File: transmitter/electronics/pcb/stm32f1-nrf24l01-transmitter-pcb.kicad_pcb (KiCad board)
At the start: 2 copper layers, 29 parts, among them K1 CONN_3, K10 CONN_3, K11 CONN_3, K2 CONN_3, K3 CONN_3, K4 CONN_3, K5 CONN_3, K6 CONN_3, K7 CONN_3, K8 CONN_3, K9 CONN_3, P1 Charge, P2 LED, P3 CONN_2, P4 CONN_2, P5 CONN_4, Q1 BC548, SW1 ON/OFF, U1 LIPO_CHARGER_+_PROTECTION, U2 STM32F103C8T6_DEV_BOARD, U3 NRF24L01P

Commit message: Work on PCB
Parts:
- removed BT1: BATTERY, PIN_ARRAY_2X1
- removed K1, K10, K11, K2, K3, K4, K5, K6, K7, K8, K9: CONN_3, PIN_ARRAY_3X1
- removed P1: Charge, PIN_ARRAY_2X1
- removed P2: LED, PIN_ARRAY_2X1
- removed P3, P4: CONN_2, PIN_ARRAY_2X1
- removed P5: CONN_4, PIN_ARRAY_4x1
- removed SW1: ON/OFF, PIN_ARRAY_2X1
- added C3: 1u, Capacitor_SMD:C_0805_2012Metric_Pad1.15x1.40mm_HandSolder, F.Cu at (154.9, 95.2)
- added C4: 1u, Capacitor_SMD:C_0805_2012Metric_Pad1.15x1.40mm_HandSolder, F.Cu at (95.2, 57.1)
- added H1: MountingHole, MountingHole:MountingHole_3.2mm_M3_DIN965, F.Cu at (182.9, 54.6)
- added H2: MountingHole, MountingHole:MountingHole_3.2mm_M3_DIN965, F.Cu at (182.9, 95.2)
- added J1: PA1/A1, Connector_JST:JST_EH_B3B-EH-A_1x03_P2.50mm_Vertical, F.Cu at (152.4, 55.9)
- added J10: PB3, Connector_JST:JST_EH_B3B-EH-A_1x03_P2.50mm_Vertical, F.Cu at (124.5, 96.5)
- added J11: PB4, Connector_JST:JST_EH_B3B-EH-A_1x03_P2.50mm_Vertical, F.Cu at (129.5, 96.5)
- added J12: PB5, Connector_JST:JST_EH_B3B-EH-A_1x03_P2.50mm_Vertical, F.Cu at (134.6, 96.5)
- added J13: PB6, Connector_JST:JST_EH_B3B-EH-A_1x03_P2.50mm_Vertical, F.Cu at (139.7, 96.5)
- added J14: PB7, Connector_JST:JST_EH_B3B-EH-A_1x03_P2.50mm_Vertical, F.Cu at (144.8, 96.5)
- added J15: PB8, Connector_JST:JST_EH_B3B-EH-A_1x03_P2.50mm_Vertical, F.Cu at (149.9, 96.5)
- added J16: PB10, Connector_JST:JST_EH_B3B-EH-A_1x03_P2.50mm_Vertical, F.Cu at (106.7, 55.9)
- added J17: PB11, Connector_JST:JST_EH_B3B-EH-A_1x03_P2.50mm_Vertical, F.Cu at (101.6, 55.9)
- added J18: USB, Connector_JST:JST_EH_B4B-EH-A_1x04_P2.50mm_Vertical, F.Cu at (118.1, 94.0)
- added J19: BATTERY, Connector_JST:JST_EH_B2B-EH-A_1x02_P2.50mm_Vertical, F.Cu at (184.2, 73.7)
- added J2: PA2/A2, Connector_JST:JST_EH_B3B-EH-A_1x03_P2.50mm_Vertical, F.Cu at (147.3, 55.9)
- added J20: UART, Connector_PinHeader_2.54mm:PinHeader_1x03_P2.54mm_Vertical, F.Cu at (96.5, 92.7)
- added J21: SWITCH, Connector_JST:JST_EH_B2B-EH-A_1x02_P2.50mm_Vertical, F.Cu at (184.2, 83.8)
- added J22: NRF24 connector, Connector_JST:JST_EH_B7B-EH-A_1x07_P2.50mm_Vertical, F.Cu at (96.5, 68.6)
- added J23: Buzzer, Connector_JST:JST_EH_B2B-EH-A_1x02_P2.50mm_Vertical, F.Cu at (170.2, 96.5)
- added J24: Meter, Connector_JST:JST_EH_B2B-EH-A_1x02_P2.50mm_Vertical, F.Cu at (158.8, 96.5)
- added J25: LED, Connector_JST:JST_EH_B2B-EH-A_1x02_P2.50mm_Vertical, F.Cu at (157.5, 61.0)
- added J26: Red, TestPoint:TestPoint_Pad_1.5x1.5mm, F.Cu at (179.1, 63.5)
- added J27: Blue, TestPoint:TestPoint_Pad_1.5x1.5mm, F.Cu at (179.1, 61.0)
- added J28: Charger LED, Connector_JST:JST_EH_B3B-EH-A_1x03_P2.50mm_Vertical, F.Cu at (184.2, 61.0)
- added J3: PA3/A3, Connector_JST:JST_EH_B3B-EH-A_1x03_P2.50mm_Vertical, F.Cu at (142.2, 55.9)
- added J4: PA4/A4, Connector_JST:JST_EH_B3B-EH-A_1x03_P2.50mm_Vertical, F.Cu at (137.2, 55.9)
- added J5: PA5/A5, Connector_JST:JST_EH_B3B-EH-A_1x03_P2.50mm_Vertical, F.Cu at (132.1, 55.9)
- added J6: PA6/A6, Connector_JST:JST_EH_B3B-EH-A_1x03_P2.50mm_Vertical, F.Cu at (127.0, 55.9)
- added J7: PA7/A7, Connector_JST:JST_EH_B3B-EH-A_1x03_P2.50mm_Vertical, F.Cu at (121.9, 55.9)
- added J8: PB0/A8, Connector_JST:JST_EH_B3B-EH-A_1x03_P2.50mm_Vertical, F.Cu at (116.8, 55.9)
- added J9: PB1/A9, Connector_JST:JST_EH_B3B-EH-A_1x03_P2.50mm_Vertical, F.Cu at (111.8, 55.9)
- added R5: 1k, Resistor_SMD:R_0805_2012Metric_Pad1.15x1.40mm_HandSolder, F.Cu at (149.9, 66.0)
- C1: value 1u -> 100nF; footprint SM0805 -> Capacitor_SMD:C_0805_2012Metric_Pad1.15x1.40mm_HandSolder; moved to F.Cu
- C2: value 100nF -> 1u; footprint SM0805 -> Capacitor_SMD:C_0805_2012Metric_Pad1.15x1.40mm_HandSolder; moved to F.Cu
- Q1: value BC548 -> BC547B; footprint TO92 -> Package_TO_SOT_SMD:SOT-23_Handsoldering
- R1: value 1k -> 22k; footprint SM0805 -> Resistor_SMD:R_0805_2012Metric_Pad1.15x1.40mm_HandSolder; moved to F.Cu
- R2: value R -> 33k; footprint SM0805 -> Resistor_SMD:R_0805_2012Metric_Pad1.15x1.40mm_HandSolder; moved to F.Cu
- R3: value R -> 1k; footprint SM0805 -> Resistor_SMD:R_0805_2012Metric_Pad1.15x1.40mm_HandSolder; moved to F.Cu
- R4: value 1k -> 3k9; footprint SM0805 -> Resistor_SMD:R_0805_2012Metric_Pad1.15x1.40mm_HandSolder; moved to F.Cu
- SP1: footprint PIN_ARRAY_2X1 -> Buzzer_Beeper:Buzzer_12x9.5RM7.6
- U1: footprint LiPo_charger_and_protection -> WLA:LiPo_charger_and_protection
- U2: footprint DIP-40__600 -> WLA:STM32F103C8T6_DEV_BOARD
- U3: footprint NRF24L01P-PA-LNA -> Connector_PinHeader_2.54mm:PinHeader_2x04_P2.54mm_Vertical; moved to F.Cu
- moved U1 168.1 mm to (170.2, 66.0), turned to 270 degrees
- moved U3 135.9 mm to (94.0, 71.1), turned to 0 degrees
- moved R1 134.7 mm to (142.2, 76.2), turned to 90 degrees
- moved R2 132.8 mm to (147.3, 76.2), turned to 270 degrees
- moved U2 132.3 mm to (127.0, 76.2)
- moved C2 121.7 mm to (160.0, 83.8), turned to 90 degrees
- moved R3 111.2 mm to (170.2, 83.8), turned to 0 degrees
- moved SP1 107.9 mm to (165.1, 91.4), turned to 0 degrees
- moved R4 103.4 mm to (156.2, 88.9)
- moved Q1 101.1 mm to (165.1, 83.8), turned to 180 degrees
- moved C1 89.1 mm to (149.9, 76.2), turned to 270 degrees
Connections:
- C1 pad 1: VCC -> /ADC0
- C2 pad 1: /ADC0 -> VDD
- Q1 pad 1: GND -> Net-(J23-Pad1)
- Q1 pad 2: N-0000013 -> Net-(Q1-Pad2)
- Q1 pad 3: N-0000014 -> GND
- R1 pad 1: N-0000043 -> VDD
- R1 pad 2: /LED -> /ADC0
- R2 pad 1: VDD -> /ADC0
- R2 pad 2: /ADC0 -> GND
- R3 pad 1: /ADC0 -> Net-(Q1-Pad2)
- R3 pad 2: GND -> /BUZZER
- R4 pad 1: /BUZZER -> /METER
- R4 pad 2: N-0000013 -> Net-(C3-Pad1)
- SP1 pad 2: N-0000014 -> Net-(J23-Pad1)
- U1 pad 4: N-0000029 -> GND
- U1 pad 5: N-000004 -> /+USB
- U1 pad 6: N-0000021 -> GND
- U2 pad 11: (no net) -> /PB3
- U2 pad 12: (no net) -> /PB4
- U2 pad 13: (no net) -> /PB5
- U2 pad 14: (no net) -> /PB6
- U2 pad 15: (no net) -> /PB7
- U2 pad 16: (no net) -> /PB8
- U2 pad 17: (no net) -> /METER
- U2 pad 20: N-0000022 -> VCC
- U2 pad 21: N-0000022 -> VCC
- U2 pad 23: (no net) -> Net-(U2-Pad23)
- U2 pad 24: (no net) -> Net-(U2-Pad24)
- U2 pad 26: /ADC1 -> /PA1/ADC1
- U2 pad 27: /ADC2 -> /PA2/ADC2
- U2 pad 28: /ADC3 -> /PA3/ADC3
- U2 pad 29: /ADC4 -> /PA4/ADC4
- U2 pad 30: /ADC5 -> /PA5/ADC5
- U2 pad 31: /ADC6 -> /PA6/ADC6
- U2 pad 32: /ADC7 -> /PA7/ADC7
- U2 pad 33: /ADC8 -> /PB0/ADC8
- U2 pad 34: /ADC9 -> /PB1/ADC9
- U2 pad 35: /SW2 -> /PB10
- U2 pad 36: /SW1 -> /PB11
- U2 pad 37: (no net) -> Net-(U2-Pad37)
- U2 pad 8: (no net) -> /USBDM
- U2 pad 9: (no net) -> /USBDP
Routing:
- net GND: track 122.4 -> 12.5 mm, vias 4 -> 0
- net VCC: track 122.5 -> 16.1 mm, vias 2 -> 0
- net /ADC0: track 20.5 -> 0.00 mm
- net N-0000022: track 15.2 -> 0.00 mm
- net N-0000014: track 15.2 -> 0.00 mm
- net VDD: track 12.4 -> 0.00 mm
- net /MISO: track 27.9 -> 16.1 mm, vias 2 -> 0
- net N-0000029: track 8.45 -> 0.00 mm
- net /SCK: track 33.0 -> 24.7 mm, vias 2 -> 0
- net N-000004: track 7.82 -> 0.00 mm
- net N-0000021: track 7.82 -> 0.00 mm
- net N-0000028: track 6.61 -> 0.00 mm
- net /SW2: track 5.08 -> 0.00 mm
- net /SW1: track 5.08 -> 0.00 mm
- net /ADC9: track 5.08 -> 0.00 mm
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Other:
- board outline added: 97.8 x 49.5 mm
- net class Default: clearance 0.1016 -> 0.2; trace_width 0.254 -> 0.25; via_dia 0.889 -> 0.8; via_drill 0.635 -> 0.4
- rule trace_clearance: 0.1016 -> 0.2
- rule trace_min: 0.254 -> 0.2
- rule via_min_drill: 0.508 -> 0.3
- rule via_min_size: 0.889 -> 0.4
- board text removed: "IMPORTANT: the nRF module is on the back side, i.e mirrored!"

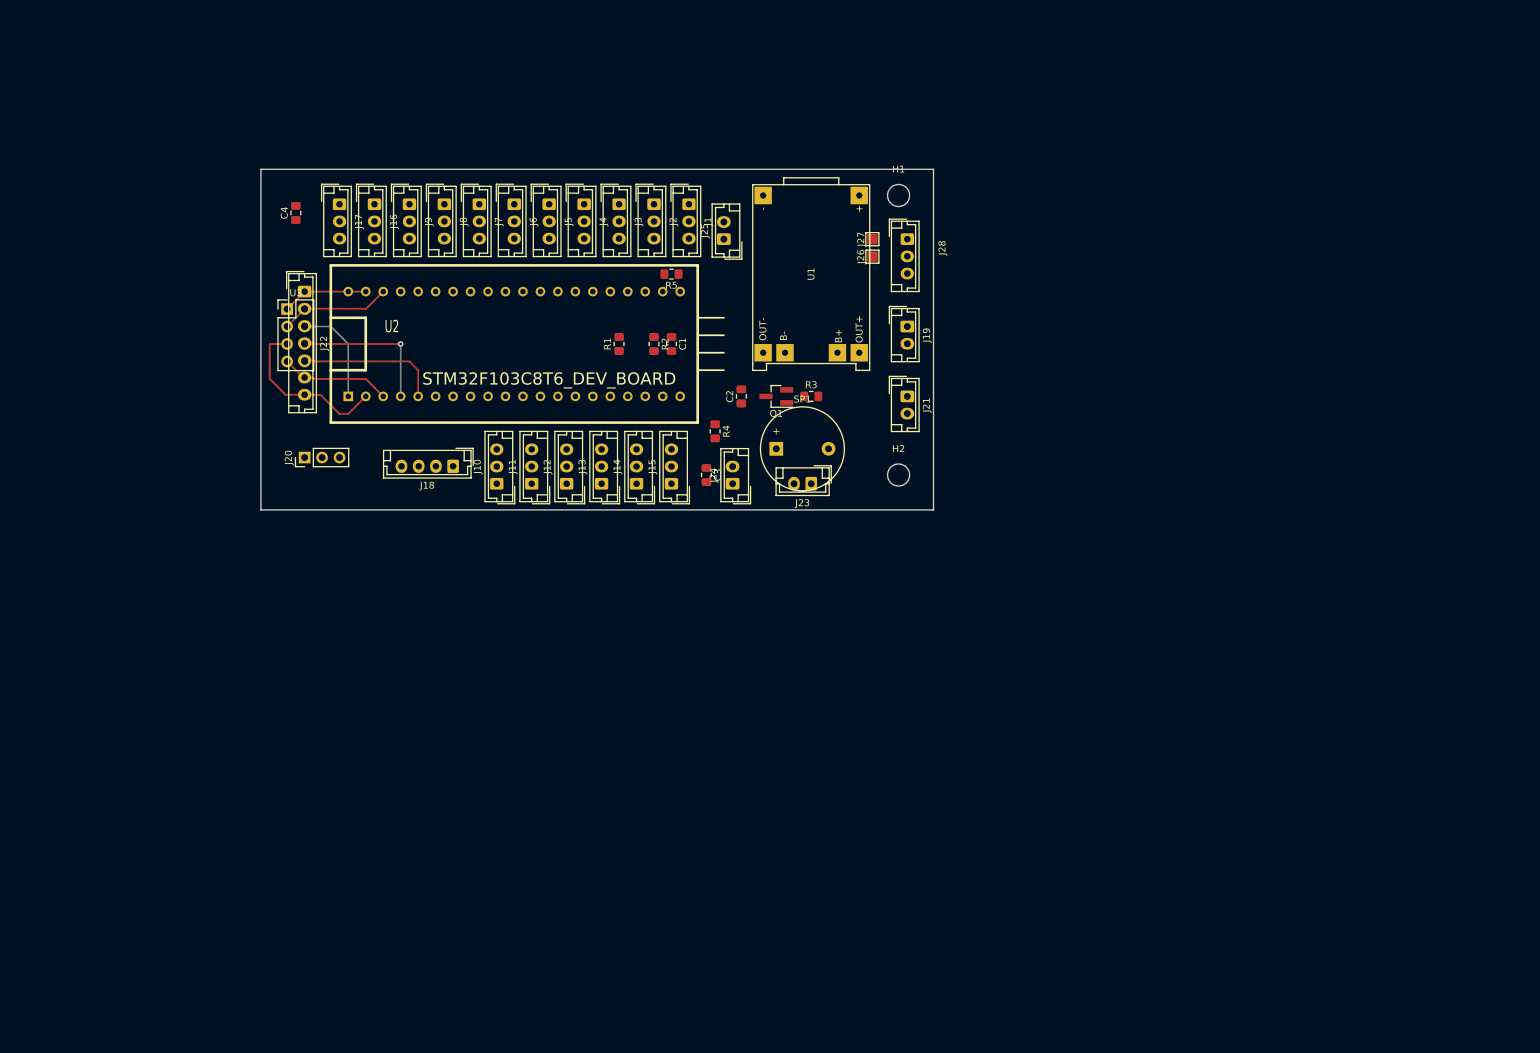
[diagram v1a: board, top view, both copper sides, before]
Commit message: Update PCB without Blue Pill, but use STM32F103 directly
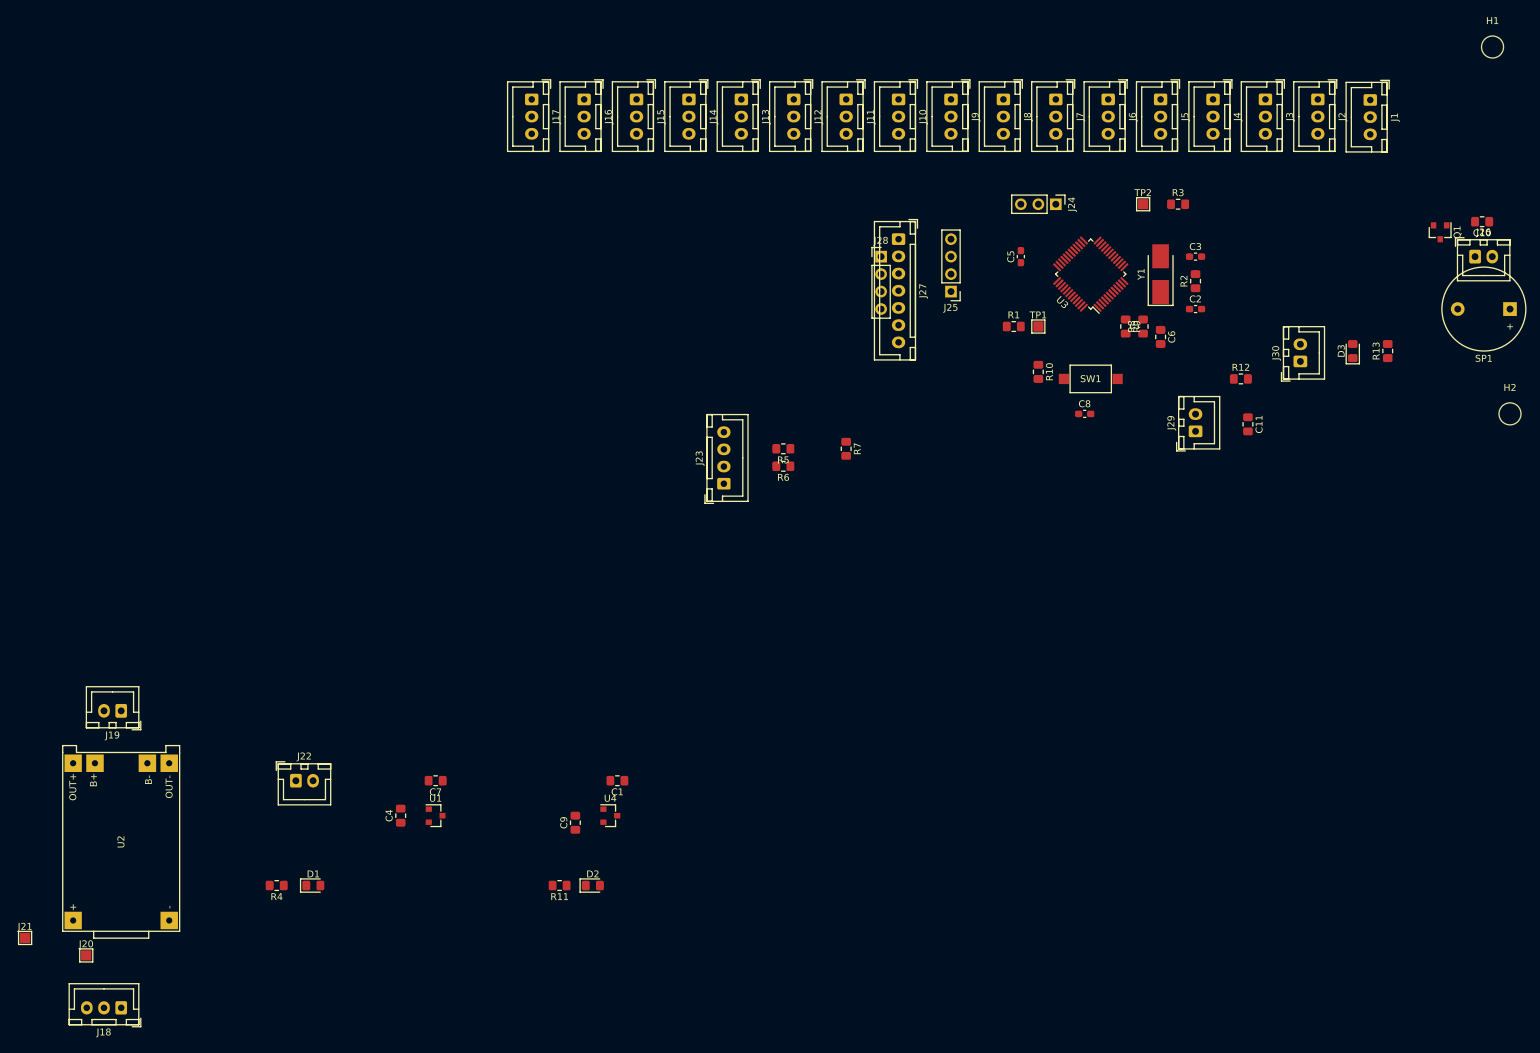
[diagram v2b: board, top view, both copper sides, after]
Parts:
- added C10: 1u, Capacitor_SMD:C_0805_2012Metric_Pad1.15x1.40mm_HandSolder, F.Cu at (267.7, 58.4)
- added C11: 1u, Capacitor_SMD:C_0805_2012Metric_Pad1.15x1.40mm_HandSolder, F.Cu at (233.7, 87.9)
- added C5: 100n, Capacitor_SMD:C_0603_1608Metric_Pad1.05x0.95mm_HandSolder, F.Cu at (200.7, 63.5)
- added C6: 100nF, Capacitor_SMD:C_0805_2012Metric_Pad1.15x1.40mm_HandSolder, F.Cu at (221.0, 75.2)
- added C7: 1u, Capacitor_SMD:C_0805_2012Metric_Pad1.15x1.40mm_HandSolder, F.Cu at (115.6, 139.7)
- added C8: 100n, Capacitor_SMD:C_0603_1608Metric_Pad1.05x0.95mm_HandSolder, F.Cu at (209.9, 86.4)
- added C9: 47u, Capacitor_SMD:C_0805_2012Metric_Pad1.15x1.40mm_HandSolder, F.Cu at (135.9, 145.8)
- added D1: LED, LED_SMD:LED_0805_2012Metric_Pad1.15x1.40mm_HandSolder, F.Cu at (97.8, 154.9)
- added D2: LED, LED_SMD:LED_0805_2012Metric_Pad1.15x1.40mm_HandSolder, F.Cu at (138.4, 154.9)
- added D3: LED, LED_SMD:LED_0805_2012Metric_Pad1.15x1.40mm_HandSolder, F.Cu at (248.9, 77.2)
- added J29: Meter, Connector_JST:JST_XH_B2B-XH-A_1x02_P2.50mm_Vertical, F.Cu at (226.1, 88.9)
- added J30: LED, Connector_JST:JST_XH_B2B-XH-A_1x02_P2.50mm_Vertical, F.Cu at (241.3, 78.7)
- added R10: 10k, Resistor_SMD:R_0805_2012Metric_Pad1.15x1.40mm_HandSolder, F.Cu at (203.2, 80.3)
- added R11: 1k5, Resistor_SMD:R_0805_2012Metric_Pad1.15x1.40mm_HandSolder, F.Cu at (133.6, 154.9)
- added R12: 3k9, Resistor_SMD:R_0805_2012Metric_Pad1.15x1.40mm_HandSolder, F.Cu at (232.7, 81.3)
- added R13: 1k, Resistor_SMD:R_0805_2012Metric_Pad1.15x1.40mm_HandSolder, F.Cu at (254.0, 77.2)
- added R6: 18, Resistor_SMD:R_0805_2012Metric_Pad1.15x1.40mm_HandSolder, F.Cu at (166.1, 94.0)
- added R7: 1K5, Resistor_SMD:R_0805_2012Metric_Pad1.15x1.40mm_HandSolder, F.Cu at (175.3, 91.4)
- added R8: 22k, Resistor_SMD:R_0805_2012Metric_Pad1.15x1.40mm_HandSolder, F.Cu at (218.4, 73.7)
- added R9: 33k, Resistor_SMD:R_0805_2012Metric_Pad1.15x1.40mm_HandSolder, F.Cu at (215.9, 73.7)
- added SW1: RESET, tact-switch:Tact switch 6x4x3, F.Cu at (210.8, 81.3)
- added TP1: BOOT0, TestPoint:TestPoint_Pad_1.5x1.5mm, F.Cu at (203.2, 73.7)
- added TP2: BOOT1, TestPoint:TestPoint_Pad_1.5x1.5mm, F.Cu at (218.4, 55.9)
- added U4: MCP1703A-3302, Package_TO_SOT_SMD:SOT-23, F.Cu at (141.0, 144.8)
- added Y1: 8MHz, Crystal:Crystal_SMD_5032-2Pin_5.0x3.2mm_HandSoldering, F.Cu at (221.0, 66.0)
- C1: value 100nF -> 1u
- C2, C3: value 1u -> 18p; footprint Capacitor_SMD:C_0805_2012Metric_Pad1.15x1.40mm_HandSolder -> Capacitor_SMD:C_0603_1608Metric_Pad1.05x0.95mm_HandSolder
- C4: value 1u -> 10u
- J1, J10, J11, J12, J13, J14, J15, J16, J17, J2, J3, J4, J5, J6, J7, J8, J9: footprint Connector_JST:JST_EH_B3B-EH-A_1x03_P2.50mm_Vertical -> Connector_JST:JST_XH_B3B-XH-A_1x03_P2.50mm_Vertical
- J18: value USB -> External charger LED; footprint Connector_JST:JST_EH_B4B-EH-A_1x04_P2.50mm_Vertical -> Connector_JST:JST_XH_B3B-XH-A_1x03_P2.50mm_Vertical
- J19: footprint Connector_JST:JST_EH_B2B-EH-A_1x02_P2.50mm_Vertical -> Connector_JST:JST_XH_B2B-XH-A_1x02_P2.50mm_Vertical
- J20: value UART -> Red; footprint Connector_PinHeader_2.54mm:PinHeader_1x03_P2.54mm_Vertical -> TestPoint:TestPoint_Pad_1.5x1.5mm
- J21: value SWITCH -> Blue; footprint Connector_JST:JST_EH_B2B-EH-A_1x02_P2.50mm_Vertical -> TestPoint:TestPoint_Pad_1.5x1.5mm
- J22: value NRF24 connector -> POWER SWITCH; footprint Connector_JST:JST_EH_B7B-EH-A_1x07_P2.50mm_Vertical -> Connector_JST:JST_XH_B2B-XH-A_1x02_P2.50mm_Vertical
- J23: value Buzzer -> USB; footprint Connector_JST:JST_EH_B2B-EH-A_1x02_P2.50mm_Vertical -> Connector_JST:JST_XH_B4B-XH-A_1x04_P2.50mm_Vertical
- J24: value Meter -> UART; footprint Connector_JST:JST_EH_B2B-EH-A_1x02_P2.50mm_Vertical -> Connector_PinHeader_2.54mm:PinHeader_1x03_P2.54mm_Vertical
- J25: value LED -> SWD; footprint Connector_JST:JST_EH_B2B-EH-A_1x02_P2.50mm_Vertical -> Connector_PinHeader_2.54mm:PinHeader_1x04_P2.54mm_Vertical
- J26: value Red -> Buzzer; footprint TestPoint:TestPoint_Pad_1.5x1.5mm -> Connector_JST:JST_XH_B2B-XH-A_1x02_P2.50mm_Vertical
- J27: value Blue -> NRF24 connector; footprint TestPoint:TestPoint_Pad_1.5x1.5mm -> Connector_JST:JST_XH_B7B-XH-A_1x07_P2.50mm_Vertical
- J28: value Charger LED -> NRF24 module; footprint Connector_JST:JST_EH_B3B-EH-A_1x03_P2.50mm_Vertical -> Connector_PinHeader_2.54mm:PinHeader_1x04_P2.54mm_Vertical
- Q1: value BC547B -> PMV30UN; footprint Package_TO_SOT_SMD:SOT-23_Handsoldering -> Package_TO_SOT_SMD:SOT-23
- R1: value 22k -> 100k
- R2: value 33k -> 10M
- R3: value 1k -> 100k
- R4: value 3k9 -> 1k5
- R5: value 1k -> 18
- U1: value LIPO_CHARGER_+_PROTECTION -> MCP1703A-3302; footprint WLA:LiPo_charger_and_protection -> Package_TO_SOT_SMD:SOT-23
- U2: value STM32F103C8T6_DEV_BOARD -> LIPO_CHARGER_+_PROTECTION; footprint WLA:STM32F103C8T6_DEV_BOARD -> WLA:LiPo_charger_and_protection
- U3: value NRF24L01P -> STM32F103CBT6; footprint Connector_PinHeader_2.54mm:PinHeader_2x04_P2.54mm_Vertical -> Package_QFP:LQFP-48_7x7mm_P0.5mm
- moved J21 150.5 mm to (55.9, 162.6), turned to 0 degrees
- moved J19 127.2 mm to (69.8, 129.5), turned to 180 degrees
- moved U3 117.0 mm to (210.8, 66.0), turned to 135 degrees
- moved SP1 108.6 mm to (271.8, 71.1), turned to 180 degrees
- moved J1 100.2 mm to (251.5, 40.7)
- moved Q1 99.4 mm to (261.6, 60.0), turned to 270 degrees
- moved J2 97.7 mm to (243.8, 40.6)
- moved U1 95.8 mm to (115.6, 144.8), turned to 0 degrees
- moved J3 95.2 mm to (236.2, 40.6)
- moved J4 92.7 mm to (228.6, 40.6)
- moved J18 92.4 mm to (69.8, 172.7)
- moved U2 92.2 mm to (69.8, 148.6), turned to 90 degrees
- moved R4 91.8 mm to (92.5, 154.9), turned to 180 degrees
- moved J5 90.2 mm to (221.0, 40.6)
- moved H2 89.3 mm to (271.8, 86.4)
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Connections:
- C1 pad 1: /ADC0 -> VDD
- C2 pad 1: VDD -> /OSCIN
- C3 pad 1: Net-(C3-Pad1) -> /OSCOUT
- C4 pad 1: VCC -> +3V3
- J1 pad 2: VCC -> +3V3
- J1 pad 3: /PA1/ADC1 -> /PA1-ADC1
- J10 pad 2: VCC -> +3V3
- J11 pad 2: VCC -> +3V3
- J12 pad 2: VCC -> +3V3
- J13 pad 2: VCC -> +3V3
- J14 pad 2: VCC -> +3V3
- J15 pad 2: VCC -> +3V3
- J16 pad 2: VCC -> +3V3
- J17 pad 2: VCC -> +3V3
- J18 pad 1: GND -> Net-(J18-Pad1)
- J18 pad 2: /USBDP -> Net-(J18-Pad2)
- J18 pad 3: /USBDM -> /+USB
- J2 pad 2: VCC -> +3V3
- J2 pad 3: /PA2/ADC2 -> /PA2-ADC2
- J20 pad 1: GND -> Net-(J18-Pad2)
- J21 pad 1: Net-(J21-Pad1) -> Net-(J18-Pad1)
- J22 pad 1: GND -> Net-(J22-Pad1)
- J22 pad 2: VCC -> VDD
- J23 pad 1: Net-(J23-Pad1) -> GND
- J23 pad 2: VDD -> Net-(J23-Pad2)
- J24 pad 2: Net-(C3-Pad1) -> /TX
- J25 pad 1: Net-(J25-Pad1) -> GND
- J25 pad 2: VCC -> /SWDCLK
- J27 pad 1: Net-(J27-Pad1) -> GND
- J28 pad 1: Net-(J27-Pad1) -> GND
- J28 pad 2: Net-(J26-Pad1) -> /CE
- J28 pad 3: /+USB -> /SCK
- J3 pad 2: VCC -> +3V3
- J3 pad 3: /PA3/ADC3 -> /PA3-ADC3
- J4 pad 2: VCC -> +3V3
- J4 pad 3: /PA4/ADC4 -> /PA4-ADC4
- J5 pad 2: VCC -> +3V3
- J5 pad 3: /PA5/ADC5 -> /PA5-ADC5
- J6 pad 2: VCC -> +3V3
- J6 pad 3: /PA6/ADC6 -> /PA6-ADC6
- J7 pad 2: VCC -> +3V3
- J7 pad 3: /PA7/ADC7 -> /PA7-ADC7
- J8 pad 2: VCC -> +3V3
- J8 pad 3: /PB0/ADC8 -> /PB0-ADC8
- J9 pad 2: VCC -> +3V3
- J9 pad 3: /PB1/ADC9 -> /PB1-ADC9
- Q1 pad 1: Net-(J23-Pad1) -> /BUZZER
- Q1 pad 2: Net-(Q1-Pad2) -> GND
- Q1 pad 3: GND -> Net-(J26-Pad1)
- R1 pad 1: VDD -> /BOOT0
- R1 pad 2: /ADC0 -> GND
- R2 pad 1: /ADC0 -> /OSCIN
- R2 pad 2: GND -> /OSCOUT
- R3 pad 1: Net-(Q1-Pad2) -> /BOOT1
- R3 pad 2: /BUZZER -> GND
- R4 pad 1: /METER -> Net-(D1-Pad1)
- R4 pad 2: Net-(C3-Pad1) -> GND
- R5 pad 1: Net-(J25-Pad1) -> /USBDM
- R5 pad 2: /LED -> Net-(J23-Pad3)
- SP1 pad 2: Net-(J23-Pad1) -> Net-(J26-Pad1)
- U1 pad 1: Net-(J19-Pad2) -> GND
- U1 pad 2: Net-(J19-Pad1) -> +3V3
- U1 pad 3: Net-(J21-Pad1) -> VDD
- U2 pad 1: /CSN -> Net-(J19-Pad2)
- U2 pad 2: /SCK -> Net-(J19-Pad1)
- U2 pad 3: /MISO -> Net-(J22-Pad1)
- U2 pad 4: /MOSI -> GND
- U2 pad 5: /IRQ -> /+USB
- U2 pad 6: /TX -> GND
- U3 pad 1: GND -> +3V3
- U3 pad 2: VCC -> /LED
- U3 pad 3: VCC -> Net-(U3-Pad3)
- U3 pad 4: /CSN -> Net-(U3-Pad4)
- U3 pad 5: /SCK -> /OSCIN
- U3 pad 6: /MOSI -> /OSCOUT
- U3 pad 7: /MISO -> /NRST
- U3 pad 8: /IRQ -> GND
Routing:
- net /SCK: track 24.7 -> 0.00 mm
- net /MOSI: track 23.0 -> 0.00 mm, vias 1 -> 0
- net /IRQ: track 20.9 -> 0.00 mm
- net VCC: track 16.1 -> 0.00 mm
- net /MISO: track 16.1 -> 0.00 mm
- net /CSN: track 15.0 -> 0.00 mm
- net GND: track 12.5 -> 0.00 mm
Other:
- board outline removed

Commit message: Work on schematics and layout
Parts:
- removed J28: NRF24 module, Connector_PinHeader_2.54mm:PinHeader_1x04_P2.54mm_Vertical
- J25: footprint Connector_PinHeader_2.54mm:PinHeader_1x04_P2.54mm_Vertical -> Connector_PinHeader_2.54mm:PinHeader_1x03_P2.54mm_Vertical
- SP1: footprint Buzzer_Beeper:Buzzer_12x9.5RM7.6 -> Buzzer_Beeper:MagneticBuzzer_PUI_AT-0927-TT-6-R
- moved J18 152.9 mm to (151.1, 43.2)
- moved J21 148.8 mm to (151.1, 48.3)
- moved J20 143.8 mm to (148.6, 48.3)
- moved R4 126.2 mm to (175.3, 59.7), turned to 270 degrees
- moved D1 125.0 mm to (174.0, 55.9), turned to 180 degrees
- moved U2 123.0 mm to (156.2, 61.0), turned to 0 degrees
- moved D2 107.1 mm to (179.1, 55.9), turned to 180 degrees
- moved R11 106.1 mm to (180.3, 59.7), turned to 270 degrees
- moved J15 104.6 mm to (236.2, 91.4), turned to 90 degrees
- moved C4 103.1 mm to (174.0, 63.5), turned to 0 degrees
- moved J22 97.1 mm to (166.4, 73.7), turned to 180 degrees
- moved J19 96.6 mm to (148.6, 73.7)
- moved U1 96.0 mm to (174.0, 68.6), turned to 270 degrees
- moved C9 92.9 mm to (179.1, 63.5), turned to 0 degrees
- moved J14 91.6 mm to (228.6, 91.4), turned to 90 degrees
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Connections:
- net /CE renamed /3V3_RF
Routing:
- net /PA1-ADC1: track 0.00 -> 45.8 mm
- net /PB11: track 0.00 -> 39.1 mm
- net /PA2-ADC2: track 0.00 -> 38.6 mm
- net /PA3-ADC3: track 0.00 -> 32.8 mm
- net /PB10: track 0.00 -> 31.7 mm
- net /PA4-ADC4: track 0.00 -> 29.8 mm
- net /PB8: track 0.00 -> 29.2 mm
- net /PB3: track 0.00 -> 28.5 mm
- net /PB1-ADC9: track 0.00 -> 25.1 mm
- net /PB7: track 0.00 -> 23.7 mm
- net /PA5-ADC5: track 0.00 -> 22.9 mm
- net /PB4: track 0.00 -> 22.0 mm
- net /PB0-ADC8: track 0.00 -> 21.4 mm
- net /PB6: track 0.00 -> 20.4 mm
- net /PA6-ADC6: track 0.00 -> 19.6 mm
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
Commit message: Work on layout
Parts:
- added H3: MountingHole, MountingHole:MountingHole_3.2mm_M3_DIN965, F.Cu at (135.0, 76.0)
- J20, J21, U2: moved to B.Cu
- Q1, U1, U4: footprint Package_TO_SOT_SMD:SOT-23 -> Package_TO_SOT_SMD:SOT-23_Handsoldering
- moved R13 80.3 mm to (183.8, 89.3), turned to 180 degrees
- moved H1 77.9 mm to (195.0, 56.5)
- moved H2 77.3 mm to (195.0, 95.5)
- moved C10 76.9 mm to (179.8, 74.1), turned to 90 degrees
- moved Q1 76.8 mm to (177.2, 85.3), turned to 90 degrees
- moved SP1 75.3 mm to (183.8, 79.7), turned to 270 degrees
- moved J26 73.0 mm to (183.8, 82.2), turned to 90 degrees
- moved C11 72.4 mm to (172.8, 86.5), turned to 180 degrees
- moved R12 71.2 mm to (172.8, 84.0), turned to 0 degrees
- moved D3 70.2 mm to (188.9, 89.3), turned to 0 degrees
- moved R1 67.7 mm to (168.3, 86.5)
- moved J30 65.9 mm to (187.0, 96.2)
- moved J6 65.2 mm to (150.2, 56.8)
- moved J7 65.2 mm to (142.5, 56.8)
- moved J16 65.2 mm to (119.7, 56.8)
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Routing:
- net +3V3: track 0.00 -> 281.4 mm, vias 0 -> 4
- net VDD: track 0.00 -> 114.1 mm, vias 0 -> 1
- net /SCK: track 0.00 -> 58.9 mm, vias 0 -> 1
- net /MISO: track 0.00 -> 54.4 mm, vias 0 -> 1
- net /IRQ: track 0.00 -> 50.9 mm, vias 0 -> 1
- net /MOSI: track 0.00 -> 50.1 mm, vias 0 -> 1
- net /CSN: track 0.00 -> 41.4 mm, vias 0 -> 1
- net /+USB: track 0.00 -> 31.0 mm
- net Net-(J19-Pad2): track 0.00 -> 30.9 mm
- net /SWDIO: track 0.00 -> 30.1 mm, vias 0 -> 1
- net /ADC0: track 0.00 -> 29.7 mm
- net /LED: track 0.00 -> 29.4 mm
- net Net-(J19-Pad1): track 0.00 -> 29.3 mm
- net /SWDCLK: track 0.00 -> 27.9 mm, vias 0 -> 1
- net Net-(J22-Pad1): track 0.00 -> 25.2 mm
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- added copper zone on B.Cu, net GND
- added copper zone on F.Cu, net GND
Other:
- board outline added: 100 x 48 mm
- board text added: "BOOT0"
- board text added: "BOOT1"
- board text added: "GND"
- board text added: "MCU"
- board text added: "ON/OFF"
- board text added: "PA1/A1"
- board text added: "PA5/A5"
- board text added: "RF"
- board text added: "RX"
- board text added: "SWCLK"
- board text added: "SWDIO"
- board text added: "TX"
